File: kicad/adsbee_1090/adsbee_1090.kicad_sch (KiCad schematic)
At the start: 72 parts, among them J1 U.FL 6GHz 50R, J2 USB_Micro-B_Receptacle, J3 Conn_02x03_Odd_Even, J4 Conn_ARM_JTAG_SWD_10, SW1 SW_Push, SW2 SW_Push, U1 AD8314, U2 BGA2818, U3 MCP6566, U4 AP2112K-3.3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

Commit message: Get PWM partially working
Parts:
- C1, C10, C11, C12, C13, C14, C15, C16, C17, C2, C20, C25, C3, C4: MPN (none) -> CC0402KRX7R7BB104; Standard Cost (none) -> 0.01
- C1: MPN (none) -> CC0402KRX7R9BB223; Standard Cost (none) -> 0.01
- C18, C19, C22, C3: MPN (none) -> CL10B105KA8NNNC; Standard Cost (none) -> 0.01
- C21: MPN (none) -> CC0603KRX7R7BB225; Standard Cost (none) -> 0.03
- C23, C24: MPN (none) -> CC0402JRNPO9BN270; Standard Cost (none) -> 0.01
- C5, C6: MPN (none) -> CC0402JRNPO9BN390; Standard Cost (none) -> 0.01
- C8: MPN (none) -> DNP
- CR1: MPN (none) -> DRTR5V0U2SR-7; Standard Cost (none) -> 0.05
- J2: MPN (none) -> 10118193-0001LF; Standard Cost (none) -> 0.10
- J3: MPN (none) -> X6521WV-2x03H-C60D30; Standard Cost (none) -> 0.06
- J4: MPN 4048 -> 20021221-00010C4LF; Standard Cost 1.95 -> 0.67
- L1: MPN (none) -> LQG18HNR10J00D; Standard Cost (none) -> 0.04
- PCB1: Standard Cost (none) -> 5.00
- R10, R11: MPN (none) -> RC0402FR-0727R4L; Standard Cost (none) -> 0.01
- R12, R13, R16, R2, R3, R4: MPN (none) -> RC0402FR-0710KL; Standard Cost (none) -> 0.01
- R14, R15, R8: MPN (none) -> RC0402FR-071KL; Standard Cost (none) -> 0.01
- R5: MPN (none) -> RC0402FR-0752R3L; Standard Cost (none) -> 0.01
- R6: MPN (none) -> RC0402FR-074K99L; Standard Cost (none) -> 0.01
- R7: MPN (none) -> RC0402FR-075K1L; Standard Cost (none) -> 0.01
- U1: MPN (none) -> AD8314ACPZ-RL7; Standard Cost (none) -> 1.97
- U2: MPN (none) -> BGA2818,115; Standard Cost (none) -> 0.14
- U3: MPN (none) -> MCP6566T-E/LT; Standard Cost (none) -> 0.48
- U5: MPN (none) -> W25Q128JVSIQ; Standard Cost (none) -> 0.37
- U6: MPN (none) -> RP2040; Standard Cost (none) -> 0.69
- Y1: value 12.000MHz 18pF -> 12.000MHz 18pF ±20ppm 80R; footprint Crystal:Crystal_SMD_SeikoEpson_FA238-4Pin_3.2x2.5mm -> Crystal:Crystal_SMD_3225-4Pin_3.2x2.5mm; MPN FA-238V 12.0000MA-C5 -> TAXM12M4RKDCDT2T; Standard Cost 0.61 -> 0.05
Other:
- note added: "Note: 1k series resistor is calculated for crystal ESR = 50Ohms, Crystal is 80Ohms."
- note removed: "Note: 1k series resistor is calculated for crystal ESR = 50Ohms, FA-238 is 100Ohms."

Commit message: Add hysteresis and begin work on Rev B PCB
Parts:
- removed C3: 1uF, Capacitor_SMD:C_0603_1608Metric, symbol Device:C
- removed C4: 0.1uF, Capacitor_SMD:C_0402_1005Metric, symbol Device:C
- removed R4: 10k, Resistor_SMD:R_0402_1005Metric, symbol Device:R_US
- added C1 (x2), C2: 0.1uF, Capacitor_SMD:C_0402_1005Metric, symbol Device:C
- added C26: 7pF, Capacitor_SMD:C_0402_1005Metric, symbol Device:C
- added C27: DNP, Capacitor_SMD:C_0402_1005Metric, symbol Device:C
- added C29: 22nF, Capacitor_SMD:C_0402_1005Metric, symbol Device:C
- added D5: 20V 1A, Diode_SMD:D_SOD-123, symbol Device:D_Schottky
- added L2: 12nH, Inductor_SMD:L_0402_1005Metric, symbol Device:L
- added Q1: BSS84, Package_TO_SOT_SMD:SOT-23, symbol Transistor_FET:BSS84
- added R1: 10k, Resistor_SMD:R_0402_1005Metric, symbol Device:R_US
- added SW3: SN74LVC1G3157, Package_TO_SOT_SMD:SOT-363_SC-70-6, symbol Custom_Analog_Switch:SN74LVC1G3157
- added TP6, TP7, TP8: TestPoint, TestPoint:TestPoint_Pad_D1.0mm, symbol Connector:TestPoint
- added U7: OPA358AIDCKR, Package_TO_SOT_SMD:SOT-363_SC-70-6, symbol Custom_Amplifier_Operational:OPA358AIDCKR
- C21: value 2.2uF -> 1uF; MPN CC0603KRX7R7BB225 -> CL10B105KA8NNNC; Standard Cost 0.03 -> 0.01
- L1: footprint Inductor_SMD:L_0603_1608Metric -> Inductor_SMD:L_0402_1005Metric; MPN LQG18HNR10J00D -> LQG15HSR10J02D
- PCB1: REV REV A -> REV B
- R5: value 52.3R -> 10k; MPN RC0402FR-0752R3L -> RC0402FR-0710KL
- R6: value 4.99k -> 115R; MPN RC0402FR-074K99L -> RC0402FR-07115RL
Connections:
- net +3V3: now also R5.2, C1.1, C1.1, C29.2, Q1.2 (S), SW3.5 (VCC), U7.6 (V+); no longer R2.1
- net DECODE: now also U7.5 (ENABLE)
- net GND: now also C1.2, C1.2, C2.2, C26.2, C27.2, SW3.2 (GND), U7.2 (V-); no longer R5.2, R6.2
- net PULSES: now also SW3.6 (S)
- net RF_DET_IN: now also C26.1, L2.1; no longer R5.1, U1.1 (RFIN)
- net RF_DET_OUT: now also U3.4 (-), U7.1 (+)
- net RF_IN: now also D1.1 (A1)
- net RF_SAW_IN: no longer D1.1 (A1)
- net 3V3_FILT_RF_DET: now reaches C3.2, L1.1, R3.1, U1.8 (VPOS)
- net RECOVERED_CLK: now reaches U6.34 (GPIO22)
- net RECOVERED_CLK: now also TP7.1
- net ~{RSSI_CLEAR}: now reaches U6.35 (GPIO23)
- net ~{RSSI_CLEAR}: now also R5.1, R6.2
- net MTL_LO_PWM: now reaches U6.36 (GPIO24)
- net MTL_LO_PWM: now also R2.2
- net MTL_HI_PWM: now reaches U6.37 (GPIO25)
- net MTL_HI_PWM: now also R1.2
- net RSSI_HOLD: now reaches U6.40 (GPIO28_ADC2)
- net RSSI_HOLD: now also C29.1, D5.2 (A), Q1.3 (D), TP8.1, U7.3 (-)
- net COMP_BIAS_DC renamed MTL_LO_BIAS
- net MTL_LO_BIAS: now also R2.1, SW3.3 (B1); no longer U3.4 (-)
- net COMP_BIAS_PWM: no longer names the net of U6.27 (GPIO16)
- removed net COMP_REF: R2.2, R6.1, TP1.1, U3.3 (+), U6.39 (GPIO27_ADC1)
- new net: D5.1 (K), U7.4
- new net: Q1.1 (G), R6.1
- new net MTL_BIAS: SW3.4 (A), TP1.1, U3.3 (+)
- new net MTL_HI_BIAS: C2.1, R1.1, SW3.1 (B2), TP6.1, U6.39 (GPIO27_ADC1)
- new net RF_DET_IN_MATCHED: C27.1, L2.2, U1.1 (RFIN)
- no-connect marks 24 -> 20
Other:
- note added: "Comparator Reference Voltages"
- note added: "Enabled during decode interval to sample RSSI of packet. Enable Time: 1.5us Disable Time: 50ns"
- note added: "Ideal peak detector circuit. Diode is too big, and leaky, but reused from power input. Peak detector holds lowest trough since using inverted AD8314 output."
- note added: "Inverted Signal IN from log amp RF detector. Super sensitive to any capacitance or load (it'll mess up the slew rate)."
- note added: "RSSI Sample and Hold"
- note removed: "Comparator Reference Voltage"
- note removed: "Inverted Signal IN from log amp RF detector."
- note removed: "PWM DAC Bias"
- moved on the sheet: C1, C17, C2, C22, C5, D1, D3, D4, J3, R13, R8, R9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

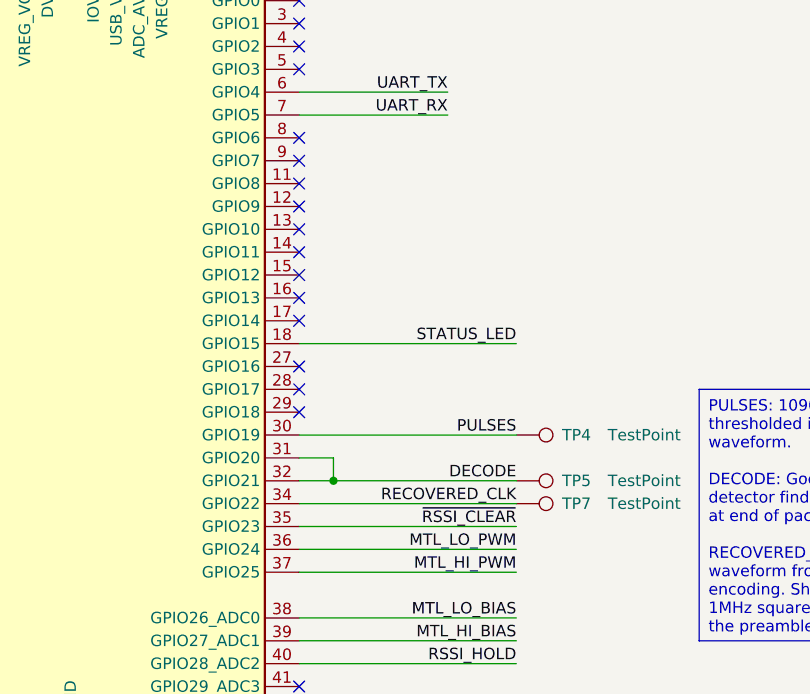
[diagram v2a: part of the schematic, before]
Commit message: Make Rev B PCB
* Add dual references for MTL hysteresis.
* Add RSSI capture circuit.
* Remove large raw files from LTSpice folder.
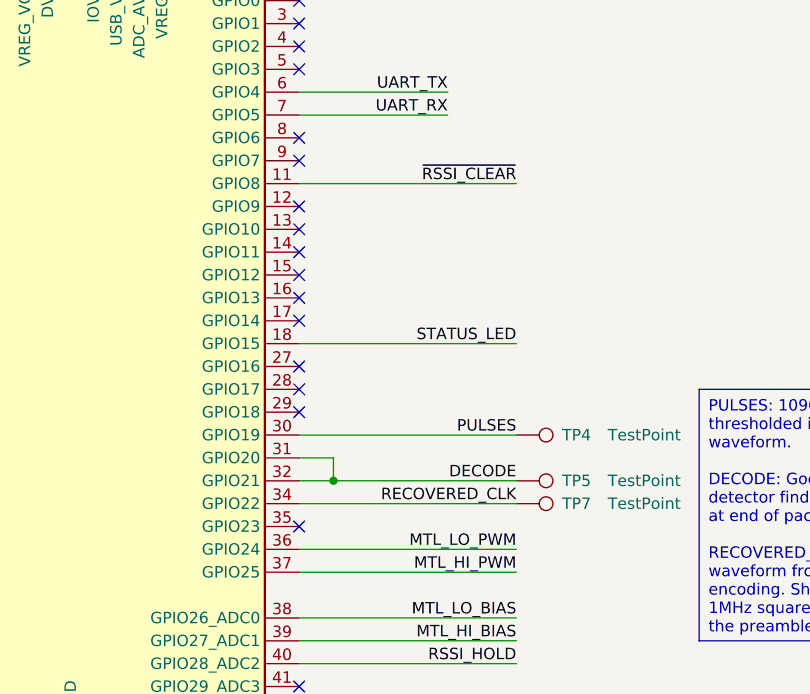
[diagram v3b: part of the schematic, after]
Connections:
- net ~{RSSI_CLEAR}: now also U6.11 (GPIO8); no longer U6.35 (GPIO23)
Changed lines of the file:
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@@
   (title_block
     (title "ADSBee")
-    (date "2023-11-25")
-    (rev "A")
+    (date "2024-01-05")
+    (rev "B")
     (company "pantsforbirds.com")
     (comment 1 "John McNelly - jkailimcnelly@gmail.com")
@@
   (no_connect (at 207.01 232.41))
   (no_connect (at 207.01 191.77))
-  (no_connect (at 207.01 176.53))
   (no_connect (at 207.01 201.93))
   (no_connect (at 207.01 156.21))
   (no_connect (at 207.01 181.61))
   (no_connect (at 207.01 196.85))
+  (no_connect (at 207.01 214.63))
   (no_connect (at 207.01 186.69))
   (no_connect (at 207.01 184.15))
@@
     (stroke (width 0) (type default))
   )
-  (wire (pts (xy 207.01 214.63) (xy 231.14 214.63))
+  (wire (pts (xy 207.01 176.53) (xy 231.14 176.53))
     (stroke (width 0) (type default))
   )
@@
     (effects (font (size 1.27 1.27)) (justify right bottom))
   )
-  (label "~{RSSI_CLEAR}" (at 231.14 214.63 180) (fields_autoplaced)
-    (effects (font (size 1.27 1.27)) (justify right bottom))
-  )
   (label "MTL_HI_PWM" (at 231.14 219.71 180) (fields_autoplaced)
     (effects (font (size 1.27 1.27)) (justify right bottom))
@@
     (effects (font (size 1.27 1.27)) (justify left bottom))
   )
+  (label "~{RSSI_CLEAR}" (at 231.14 176.53 180) (fields_autoplaced)
+    (effects (font (size 1.27 1.27)) (justify right bottom))
+  )
   (label "UART_TX" (at 223.52 166.37 180) (fields_autoplaced)

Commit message: Revise hardware for Rev B and add more software
* Redo comparator circuit with an analog switch hysteresis comparator
  thingy.
* Set up new development docker container based on a much cleaner
  pico-docker docker compose file (haven't yet gotten rid of the unused
  submodule files).
* Start working on AT command parser library in firmware that uses
  modern c++ strings.
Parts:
- Q1: MPN (none) -> BSS84; Standard Cost (none) -> 0.14
- U7: MPN (none) -> OPA358AIDCKR; Standard Cost (none) -> 0.68
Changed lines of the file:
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@@
       (effects (font (size 1.27 1.27)) hide)
     )
-    (property "MPN" "" (at 386.08 123.19 0)
-      (effects (font (size 1.27 1.27)) hide)
-    )
-    (property "Standard Cost" "" (at 386.08 123.19 0)
+    (property "MPN" "OPA358AIDCKR" (at 386.08 123.19 0)
+      (effects (font (size 1.27 1.27)) hide)
+    )
+    (property "Standard Cost" "0.68" (at 386.08 123.19 0)
       (effects (font (size 1.27 1.27)) hide)
     )
@@
       (effects (font (size 1.27 1.27)) (justify left) hide)
     )
-    (pin "1")
+    (property "MPN" "BSS84" (at 435.61 115.57 0)
+      (effects (font (size 1.27 1.27)) hide)
+    )
+    (property "Standard Cost" "0.14" (at 435.61 115.57 0)
+      (effects (font (size 1.27 1.27)) hide)
+    )
+    (pin "1")
